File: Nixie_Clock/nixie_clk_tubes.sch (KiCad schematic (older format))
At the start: 50 parts, among them Y1 IN-14, Y2 IN-14, Y3 IN-14, Y4 IN-14, Y5 IN-14, Y6 IN-14

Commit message: Almost done with uC page
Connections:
- wire segments 248 -> 210

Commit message: Added HV5122 and RaspPi
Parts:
- removed Q? (x18): BSS131, TO_SOT_Packages_SMD:SOT-23, symbol BSS131
- removed Q? (x6): FMMT596, symbol FMMT596
- removed R? (x6): R, Resistors_SMD:R_1210, symbol R
- removed R? (x12): R, symbol R
- removed Y? (x2): nixie_colon, symbol nixie_colon
- added C? (x2): 100nF, symbol C
- added R? (x8): R, symbol R
- added U? (x2): HV5112, symbol HV5112
- added Y7, Y8: nixie_colon, symbol nixie_colon
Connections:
- net labels added: CLK, DATA_IN, OE, PP5V, STR, Y1K0, Y1K1, Y1K2, Y1K3, Y1K4, Y1K5, Y1K6, Y1K7, Y1K8, Y1K9, Y2K0, Y2K1, Y2K2, Y2K3, Y2K4, Y2K5, Y2K6, Y2K7, Y2K8, Y2K9, Y3K0, Y3K1, Y3K2, Y3K3, Y3K4, Y3K5, Y3K6, Y3K7, Y3K8, Y3K9, Y4K0, Y4K1, Y4K2, Y4K3, Y4K4, Y4K5, Y4K6, Y4K7, Y4K8, Y4K9, Y5K0, Y5K1, Y5K2, Y5K3, Y5K4, Y5K5, Y5K6, Y5K7, Y5K8, Y5K9, Y6K0, Y6K1, Y6K2, Y6K3, Y6K4, Y6K5, Y6K6, Y6K7, Y6K8, Y6K9, Y7K1, Y7K2, Y8K1, Y8K2
- net labels removed: A1, A2, GA1, GA2, GA3, GA4, GA5, GA6, GK0, GK1, GK2, GK3, GK4, GK5, GK6, GK7, GK8, GK9, K0, K1, K2, K3, K4, K5, K6, K7, K8, K9, KC, KC1, KC2, YA1, YA2, YA3, YA4, YA5, YA6
- wire segments 210 -> 209
- no-connect marks 2 -> 21
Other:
- note removed: "HH:MM:SS\n"
- moved on the sheet: Y1

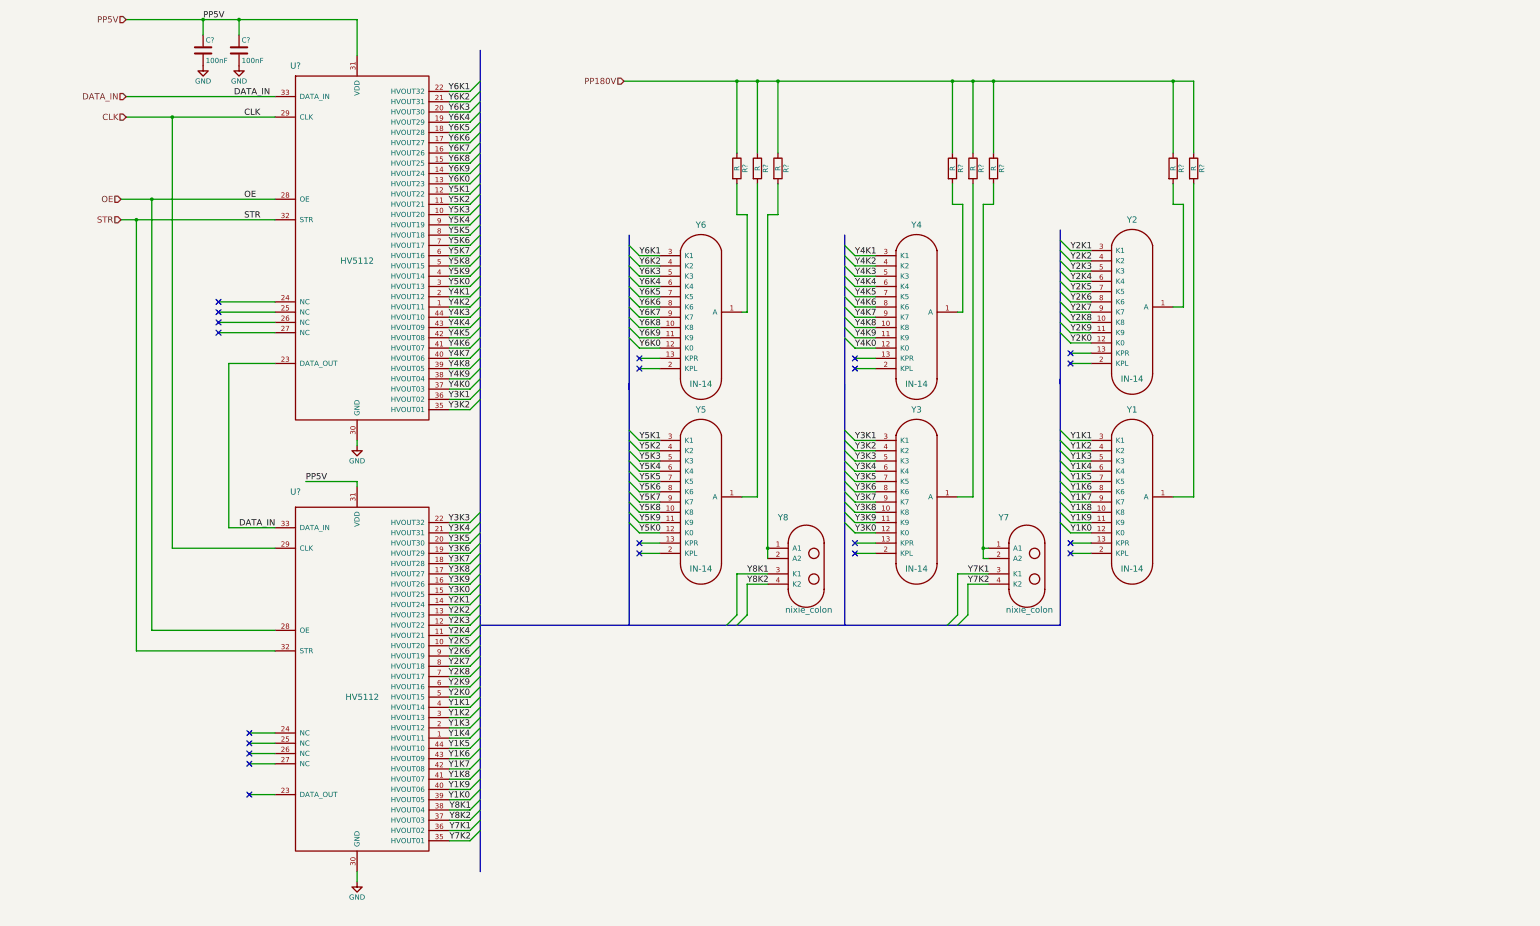
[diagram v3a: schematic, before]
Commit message: Added PIC16 instead of RaspBerry PI
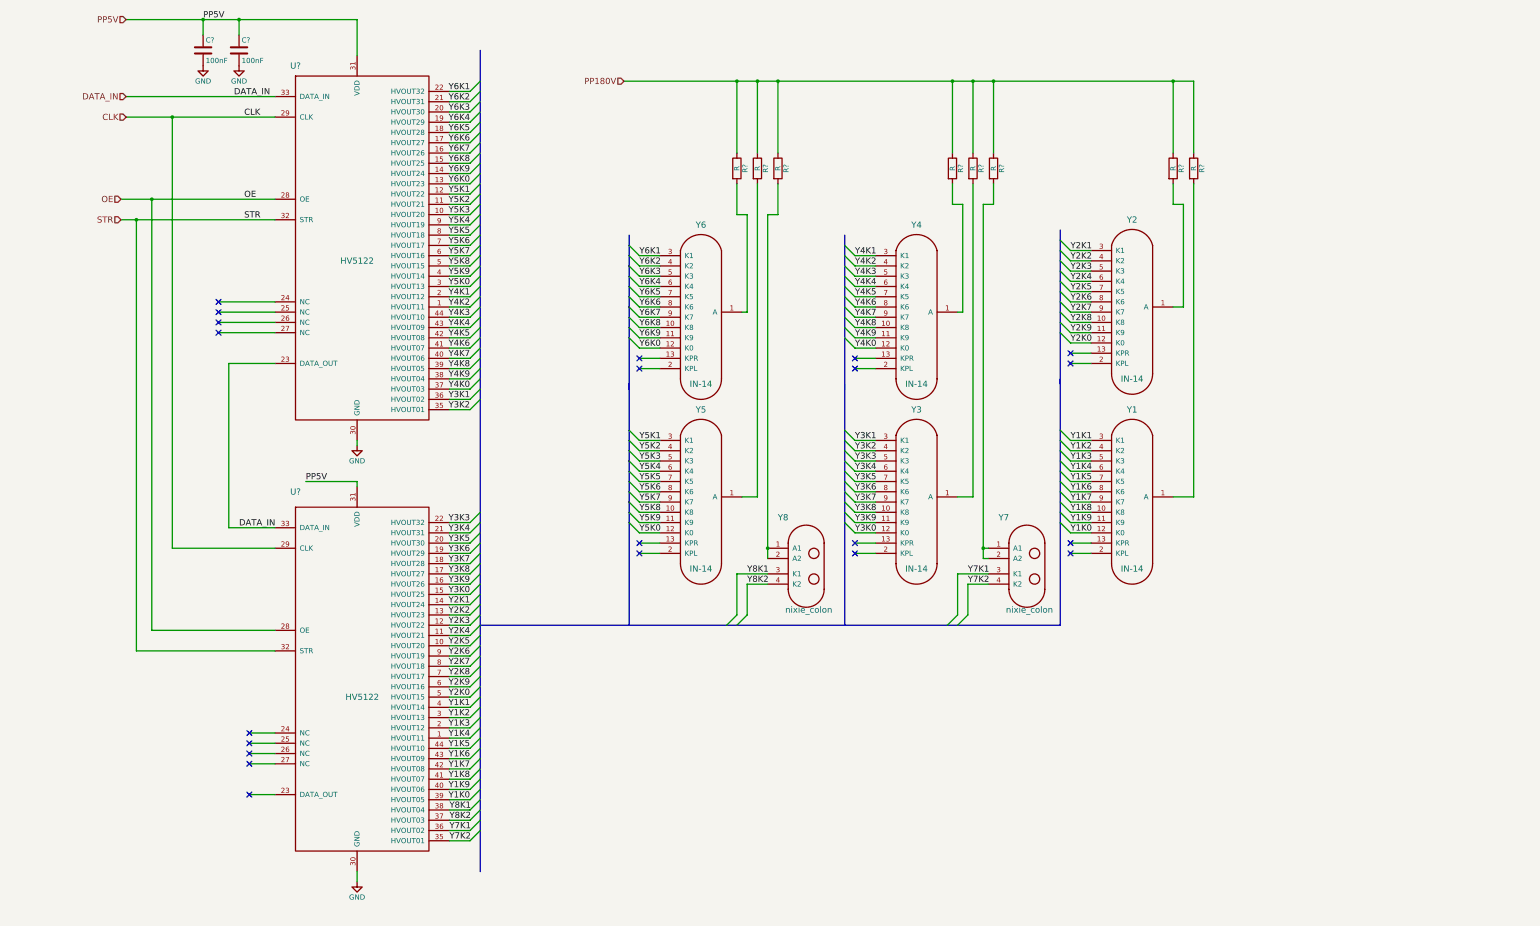
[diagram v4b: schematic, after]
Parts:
- U? (x2): value HV5112 -> HV5122
